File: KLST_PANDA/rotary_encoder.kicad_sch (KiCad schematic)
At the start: 10 parts, among them SW3 ENCODER

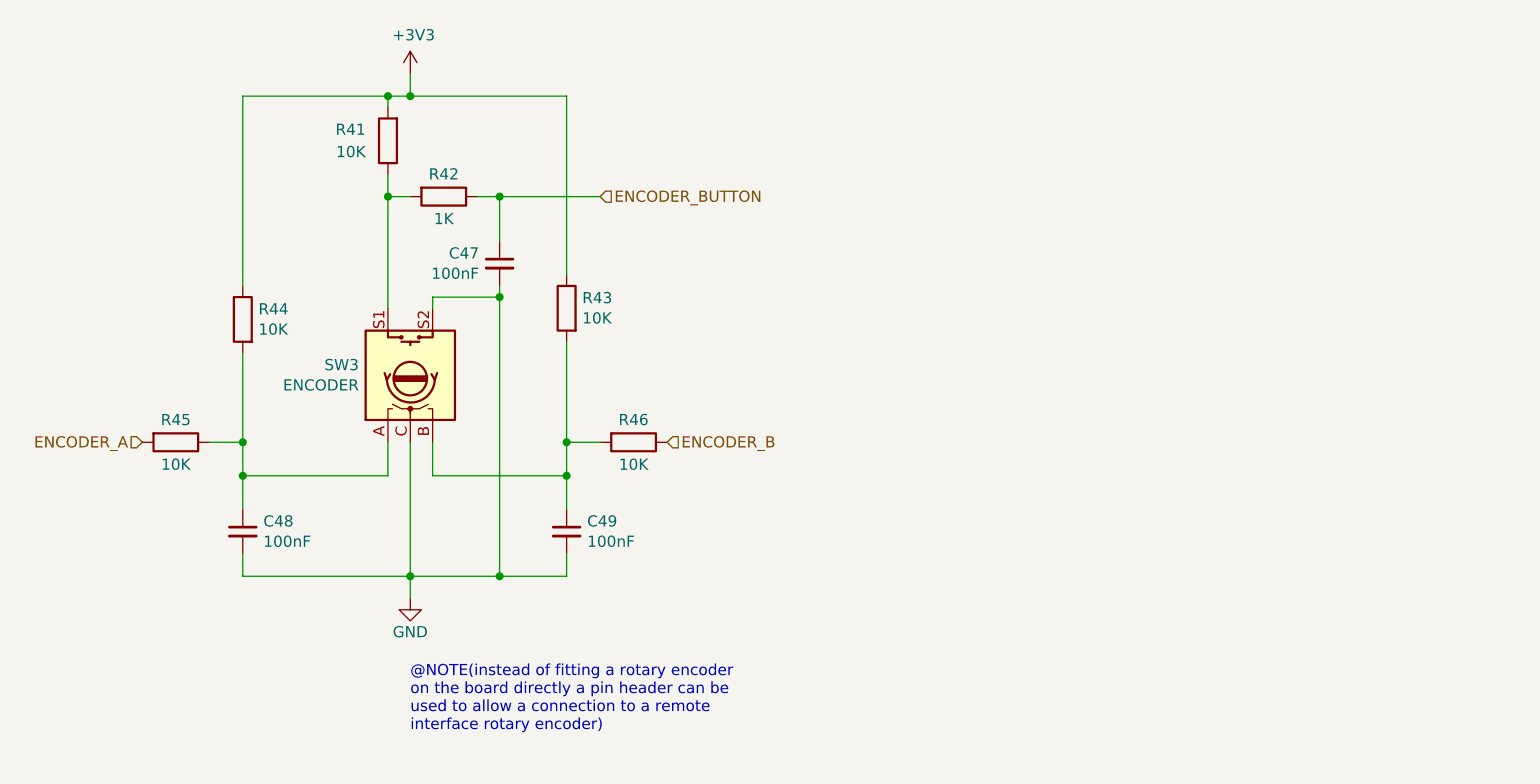
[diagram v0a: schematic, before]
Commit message: updated pin names, configured all pins and most peripherals,
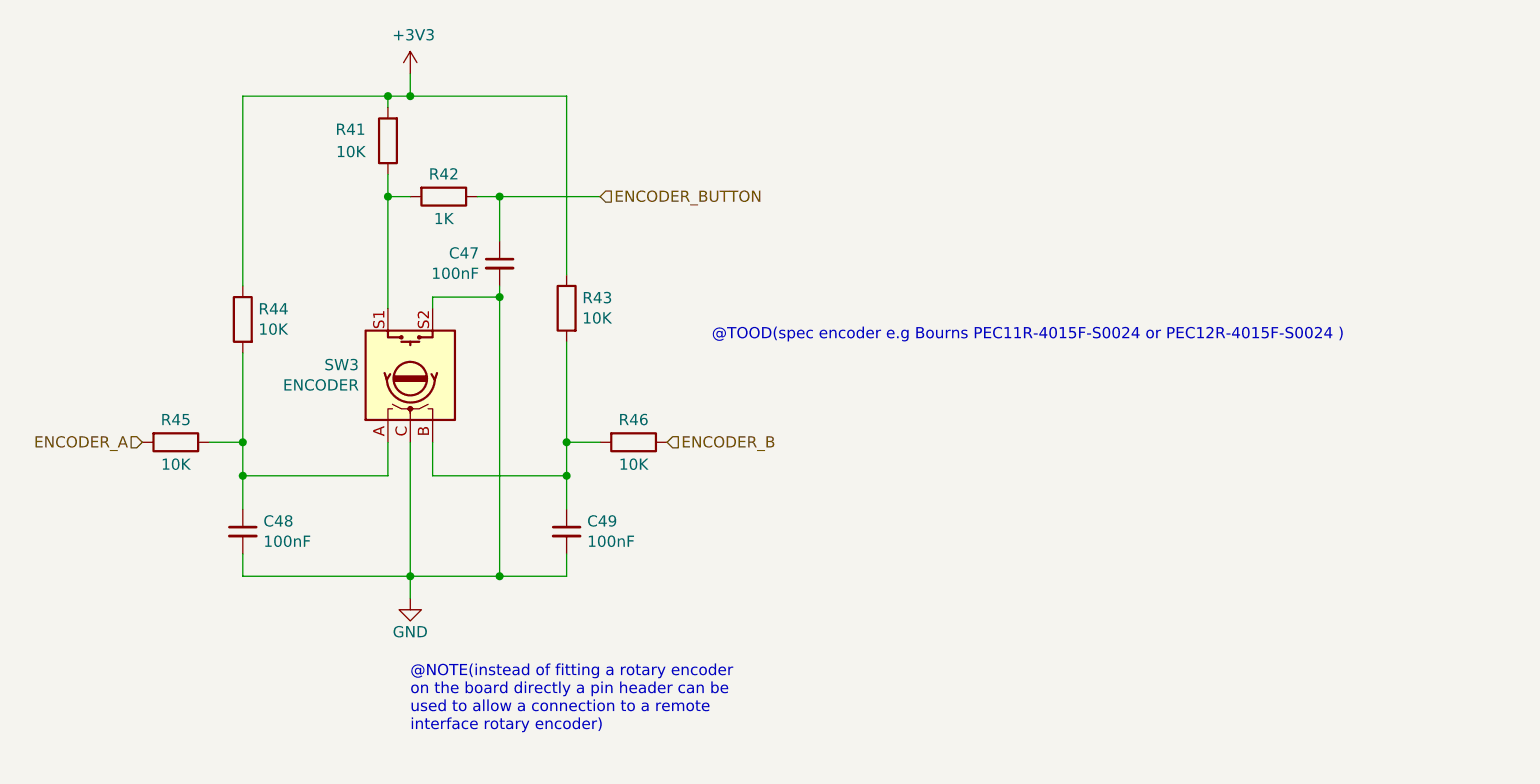
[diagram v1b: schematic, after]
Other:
- note added: "@TOOD(spec encoder e.g Bourns PEC11R-4015F-S0024 or PEC12R-4015F-S0024 )"

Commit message: improved GPIO, updated schematics
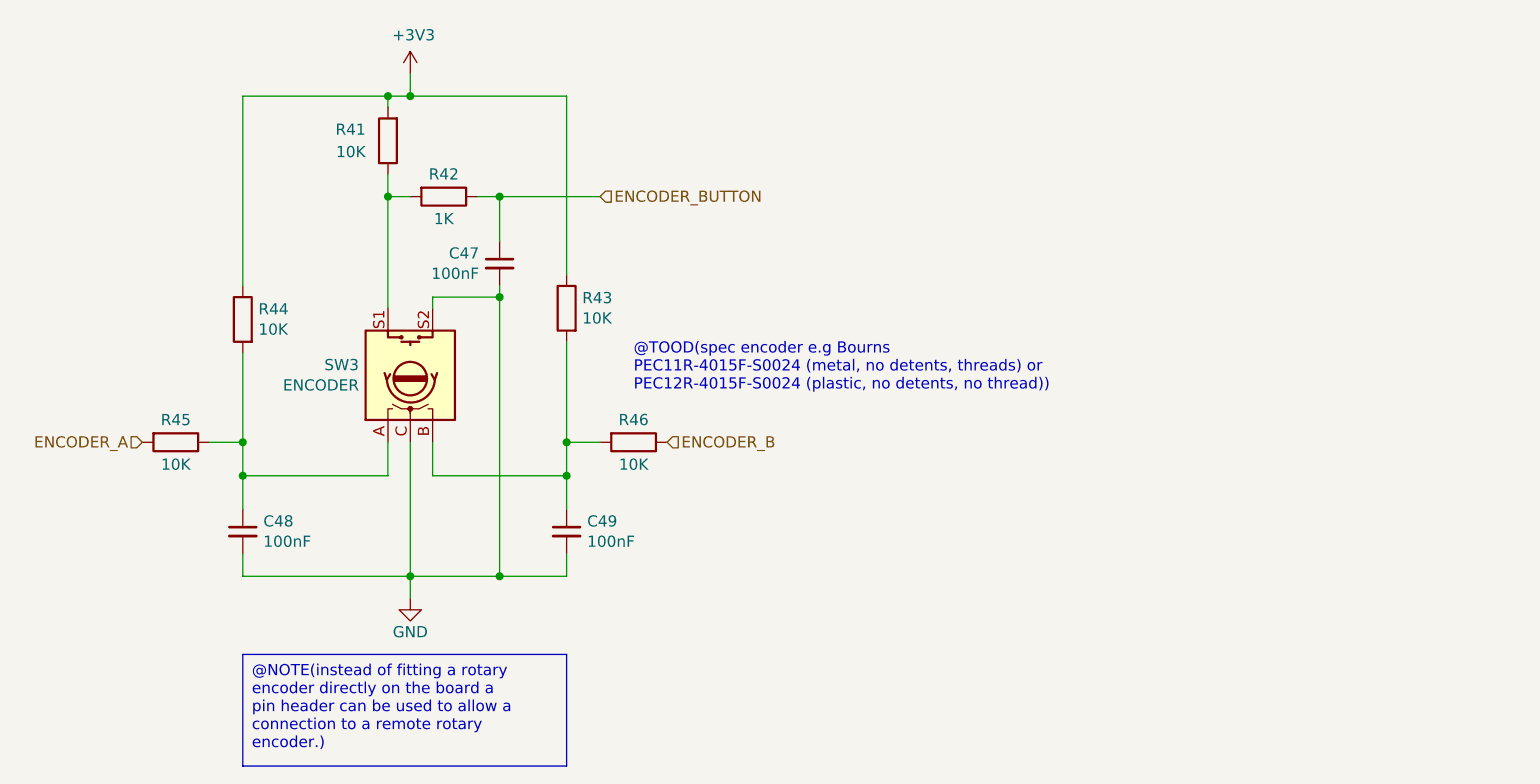
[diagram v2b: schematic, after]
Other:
- note added: "@TOOD(spec encoder e.g Bourns PEC11R-4015F-S0024 (metal, no detents, threads) or PEC12R-4015F-S0024 (plastic, no detents, no thread))"
- note removed: "@NOTE(instead of fitting a rotary encoder on the board directly a pin header can be used to allow a connection to a remote interface rotary encoder)"
- note removed: "@TOOD(spec encoder e.g Bourns PEC11R-4015F-S0024 or PEC12R-4015F-S0024 )"

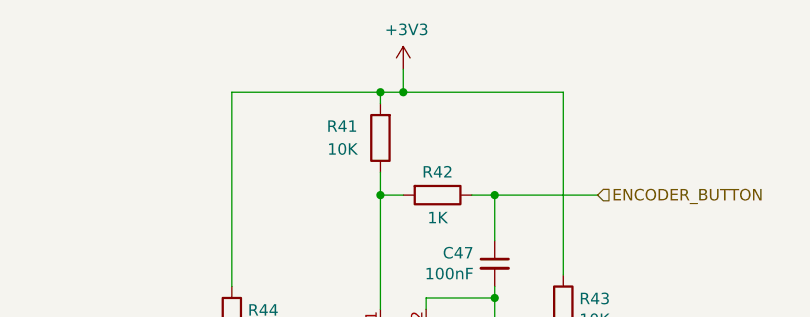
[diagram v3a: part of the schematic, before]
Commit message: started cleaning up schematic ( addressing DRC errors/warning ) (WIP)
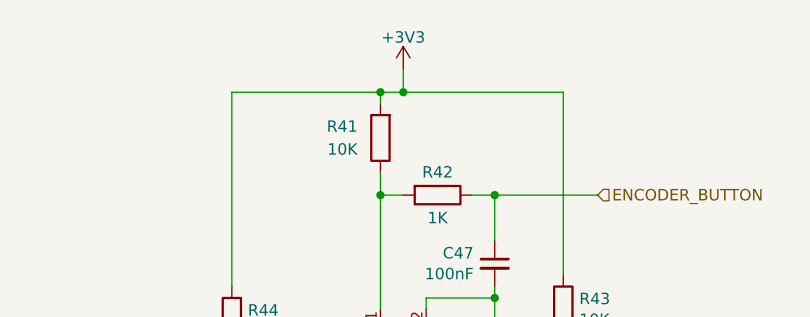
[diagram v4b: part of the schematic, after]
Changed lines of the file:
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@@
         )
         (path "/b4513875-4c57-4720-bcc5-43ead67fe18f/b123f5e9-cc72-42aa-83b5-20f52795babc/87cd59e0-a7cb-4402-bde3-1e8396956bda"
-          (reference "#PWR057") (unit 1)
-        )
-        (path "/b4513875-4c57-4720-bcc5-43ead67fe18f/b123f5e9-cc72-42aa-83b5-20f52795babc/ed61e32f-240e-4d2b-b2a8-d00b0710740e"
-          (reference "#PWR059") (unit 1)
+          (reference "#PWR058") (unit 1)
+        )
+        (path "/b4513875-4c57-4720-bcc5-43ead67fe18f/b123f5e9-cc72-42aa-83b5-20f52795babc/ed61e32f-240e-4d2b-b2a8-d00b0710740e"
+          (reference "#PWR060") (unit 1)
         )
       )
@@
       (effects (font (size 1.27 1.27)) hide)
     )
-    (property "Value" "+3V3" (at 150.241 66.7258 0)
+    (property "Value" "+3V3" (at 149.86 67.564 0)
       (effects (font (size 1.27 1.27)))
     )
@@
         )
         (path "/b4513875-4c57-4720-bcc5-43ead67fe18f/b123f5e9-cc72-42aa-83b5-20f52795babc/87cd59e0-a7cb-4402-bde3-1e8396956bda"
-          (reference "#PWR056") (unit 1)
-        )
-        (path "/b4513875-4c57-4720-bcc5-43ead67fe18f/b123f5e9-cc72-42aa-83b5-20f52795babc/ed61e32f-240e-4d2b-b2a8-d00b0710740e"
-          (reference "#PWR058") (unit 1)
-        )
-      )
+          (reference "#PWR057") (unit 1)
+        )
+        (path "/b4513875-4c57-4720-bcc5-43ead67fe18f/b123f5e9-cc72-42aa-83b5-20f52795babc/ed61e32f-240e-4d2b-b2a8-d00b0710740e"
+          (reference "#PWR059") (unit 1)
+        )
+      )

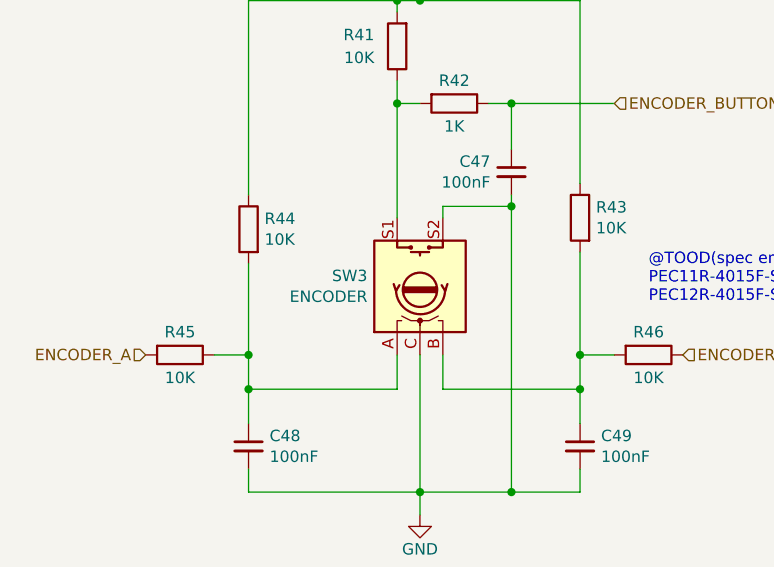
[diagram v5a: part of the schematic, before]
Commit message: updated encoder symbol, ignored simulation errors
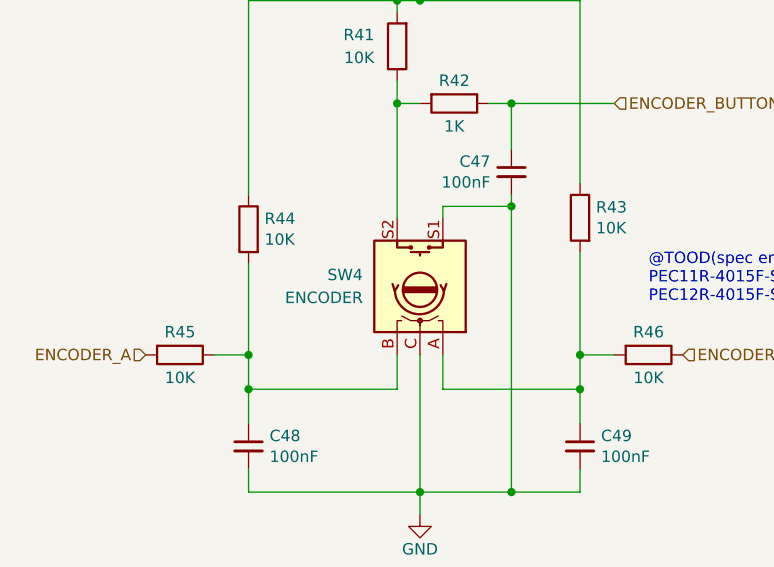
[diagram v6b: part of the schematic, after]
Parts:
- removed SW3: ENCODER, Rotary_Encoder:RotaryEncoder_Alps_EC12E-Switch_Vertical_H20mm, symbol KLST_SHEEP-rescue:Rotary_Encoder_Switch-Device
- added SW4: ENCODER, symbol Device:RotaryEncoder_Switch
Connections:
- net GND: now also SW4.C, SW4.S1
- net at R41.1, R42.2: now also SW4.S2
- net at C49.1, R43.2, R46.2: now also SW4.A
- net at C48.1, R44.2, R45.1: now also SW4.B
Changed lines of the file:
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@@
+    )
+  )
+  (symbol (lib_id "Device:RotaryEncoder_Switch") (at 149.86 105.41 270) (mirror x) (unit 1)
+    (in_bom yes) (on_board yes) (dnp no)
+    (property "Reference" "SW4" (at 143.51 104.14 90)
+      (effects (font (size 1.27 1.27)) (justify right))
+    )
+    (property "Value" "ENCODER" (at 143.51 106.68 90)
+      (effects (font (size 1.27 1.27)) (justify right))
+    )
+    (property "Footprint" "" (at 153.924 109.22 0)
+      (effects (font (size 1.27 1.27)) hide)
+    )
+    (property "Datasheet" "~" (at 156.464 105.41 0)
+      (effects (font (size 1.27 1.27)) hide)
+    )
+    (pin "A")
+    (pin "B")
+    (pin "C")
+    (pin "S1")
+    (pin "S2")
+    (instances
+      (project "KLST_PANDA"
+        (path "/b4513875-4c57-4720-bcc5-43ead67fe18f/b123f5e9-cc72-42aa-83b5-20f52795babc/87cd59e0-a7cb-4402-bde3-1e8396956bda"
+          (reference "SW4") (unit 1)
+        )
+        (path "/b4513875-4c57-4720-bcc5-43ead67fe18f/b123f5e9-cc72-42aa-83b5-20f52795babc/ed61e32f-240e-4d2b-b2a8-d00b0710740e"
+          (reference "SW5") (unit 1)
+        )
+      )
     )
   )
@@
         )
       )
-    )
-  )
-  (symbol (lib_id "KLST_SHEEP-rescue:Rotary_Encoder_Switch-Device") (at 149.86 105.41 90) (unit 1)
-    (in_bom yes) (on_board yes) (dnp no)
-    (property "Reference" "SW3" (at 144.018 104.2416 90)
-      (effects (font (size 1.27 1.27)) (justify left))
-    )
-    (property "Value" "ENCODER" (at 144.018 106.553 90)
-      (effects (font (size 1.27 1.27)) (justify left))
-    )
-    (property "Footprint" "Rotary_Encoder:RotaryEncoder_Alps_EC12E-Switch_Vertical_H20mm" (at 145.796 109.22 0)
-      (effects (font (size 1.27 1.27)) hide)
-    )
-    (property "Datasheet" "~" (at 143.256 105.41 0)
-      (effects (font (size 1.27 1.27)) hide)
-    )
-    (property "MFR.Part #" "DNF" (at 149.86 105.41 90)
-      (effects (font (size 1.27 1.27)) hide)
-    )
-    (property "Extended Part" "-" (at 149.86 105.41 0)
-      (effects (font (size 1.27 1.27)) hide)
-    )
-    (property "LCSC Part #" "" (at 149.86 105.41 0)
-      (effects (font (size 1.27 1.27)) hide)
-    )
-    (property "JLCPCB Part #" "DNF" (at 149.86 105.41 0)
-      (effects (font (size 1.27 1.27)) hide)
-    )
-    (pin "A")
-    (pin "B")
-    (pin "C")
-    (pin "S1")
-    (pin "S2")
-    (instances
-      (project "KLST_SHEEP"
-        (path "/7c1fd6fc-5c53-4ccb-a456-46fe6fc0bc71/00000000-0000-0000-0000-000060628872"
-          (reference "SW3") (unit 1)
-        )
-        (path "/7c1fd6fc-5c53-4ccb-a456-46fe6fc0bc71/00000000-0000-0000-0000-00006075a95b"
-          (reference "SW4") (unit 1)
-        )
-      )
-      (project "KLST_PANDA"
-        (path "/b4513875-4c57-4720-bcc5-43ead67fe18f/b123f5e9-cc72-42aa-83b5-20f52795babc"
-          (reference "SW?") (unit 1)
-        )
-        (path "/b4513875-4c57-4720-bcc5-43ead67fe18f/b123f5e9-cc72-42aa-83b5-20f52795babc/87cd59e0-a7cb-4402-bde3-1e8396956bda"
-          (reference "SW4") (unit 1)
-        )
-        (path "/b4513875-4c57-4720-bcc5-43ead67fe18f/b123f5e9-cc72-42aa-83b5-20f52795babc/ed61e32f-240e-4d2b-b2a8-d00b0710740e"
-          (reference "SW5") (unit 1)
-        )
-      )
